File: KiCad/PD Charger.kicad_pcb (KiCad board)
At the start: 4 copper layers, 75 x 40 mm, 89 parts, among them J1 USB_C_Receptacle_USB2.0, J2 Conn_ARM_SWD_TagConnect_TC2030, J3 XT60_M, Q1 NMOS, Q2 NMOS, Q3 NMOS, Q4 NMOS, Q5 NTMFS002P03, Q6 NTMFS002P03, Q7 Q_Dual_NMOS_S1G1D2S2G2D1, Q8 Q_Dual_NMOS_S1G1D2S2G2D1, SW1 SW_MEC_5G, U1 FUSB302B01MPX, U2 LMR36006BRNXT, U3 LT8390xFE, U4 STM32G431C6Ux

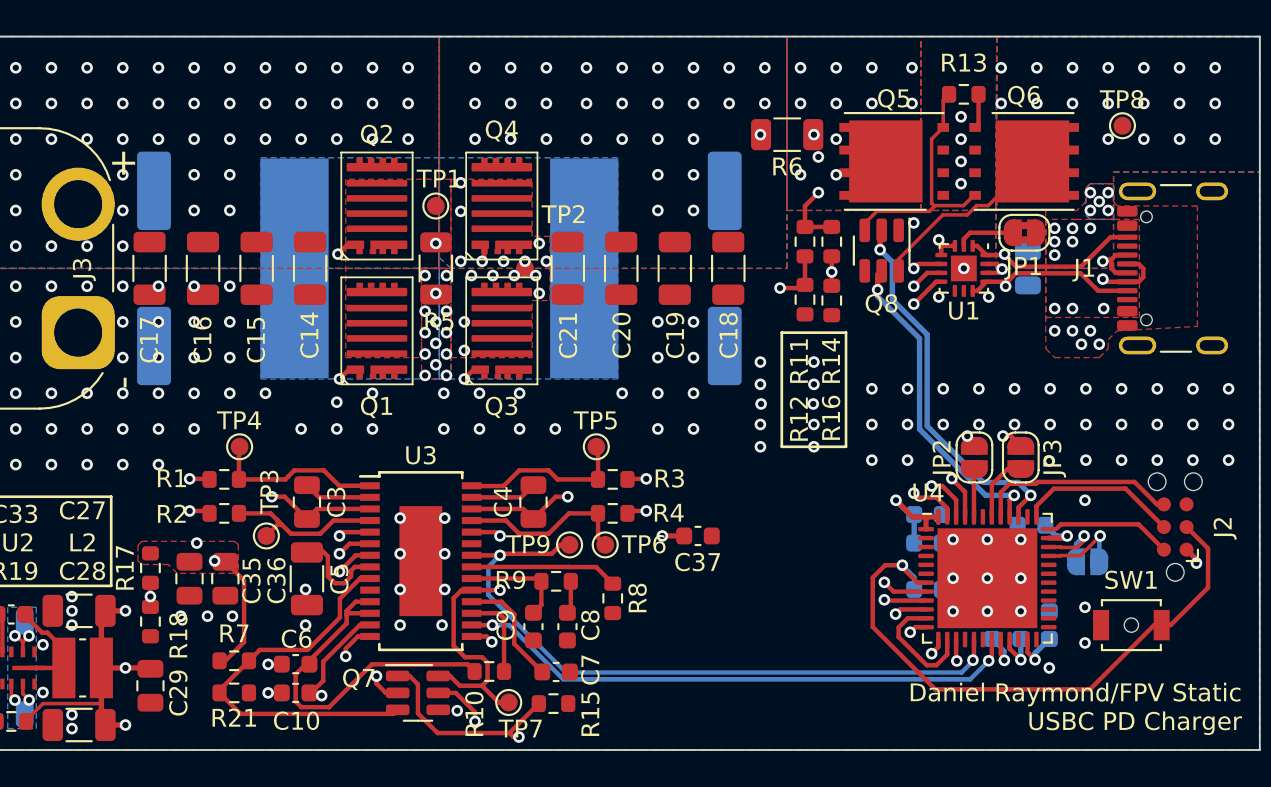
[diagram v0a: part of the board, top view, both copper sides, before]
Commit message: board update from tested issues
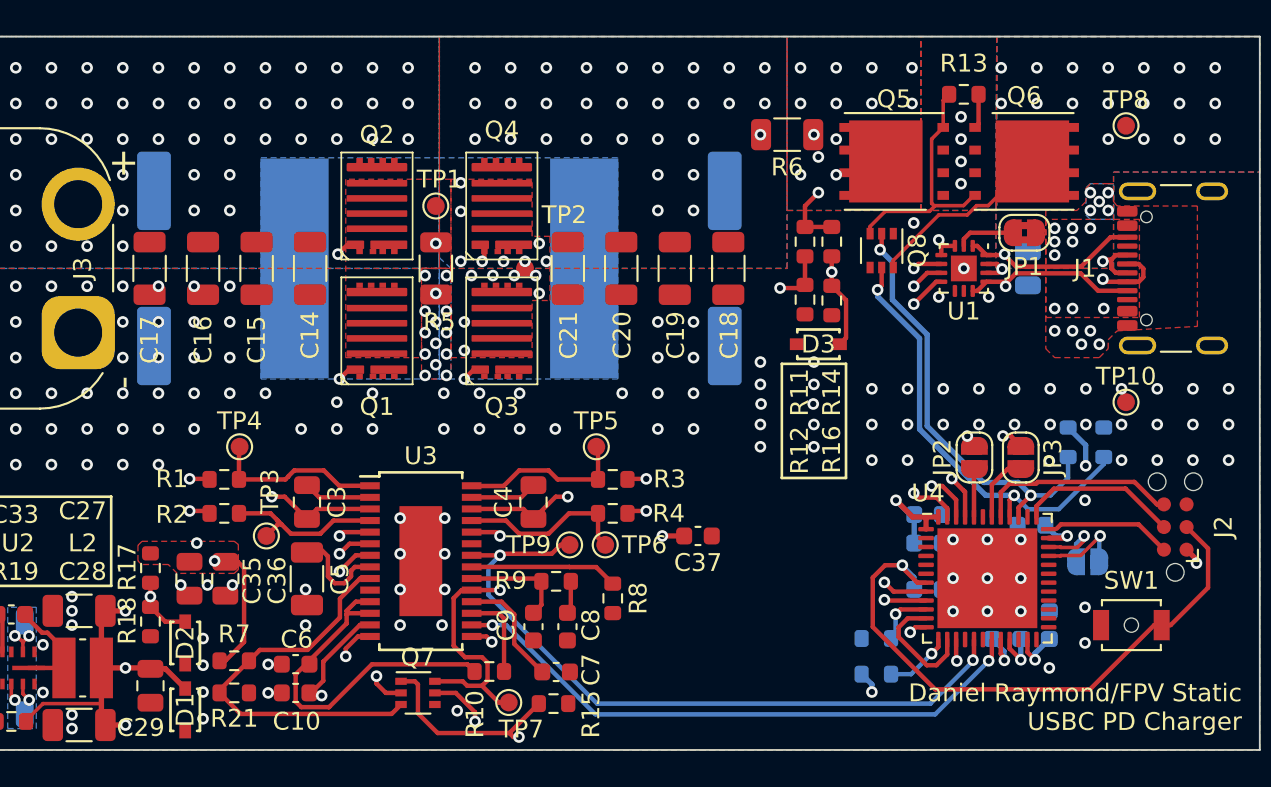
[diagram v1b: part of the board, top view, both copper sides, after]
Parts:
- added D1: 3.425, Library:CR_PLZ5V1C_VIS, F.Cu at (26.8, 49.8)
- added D2: 3.425, Library:CR_PLZ5V1C_VIS, F.Cu at (26.8, 46.0)
- added D3: 3.425, Library:CR_PLZ5V1C_VIS, F.Cu at (62.2, 29.2)
- added R22: 100k, Resistor_SMD:R_0603_1608Metric, B.Cu at (78.2, 34.8)
- added R23: 100k, Resistor_SMD:R_0603_1608Metric, B.Cu at (76.2, 34.8)
- added R24: 100k, Resistor_SMD:R_0603_1608Metric, B.Cu at (65.5, 47.8)
- added R25: 100k, Resistor_SMD:R_0603_1608Metric, B.Cu at (65.5, 45.8)
- added TP10: TestPoint_Small, TestPoint:TestPoint_Pad_D1.0mm, F.Cu at (79.5, 32.5)
- Q7, Q8: footprint Package_TO_SOT_SMD:SOT-23-6 -> Package_TO_SOT_SMD:SOT-363_SC-70-6
- moved TP8 0.20 mm to (79.5, 17.0)
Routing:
- net +3V3: track 128.1 -> 146.2 mm, vias 10 -> 12
- net /LOADEN: track 18.1 -> 25.1 mm
- net /VOUT_SENSE: track 24.1 -> 27.9 mm
- net /OUTDIS: track 21.0 -> 24.5 mm
- net /~{RUN}: track 31.2 -> 33.9 mm
- net /VIN_SENSE: track 48.7 -> 51.0 mm
- net /ISMON: track 31.9 -> 33.6 mm
- net /VCTRLV: track 34.2 -> 35.7 mm
- net /SYNC: track 38.7 -> 40.1 mm
- net GND: vias 160 -> 163

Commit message: board update
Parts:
- added R26: 10k, Resistor_SMD:R_0603_1608Metric, F.Cu at (85.2, 39.0)
- added R27: 10k, Resistor_SMD:R_0603_1608Metric, F.Cu at (85.2, 42.2)
- added SW2: SW_MEC_5G, Button_Switch_SMD:SW_SPST_B3U-1000P-B, F.Cu at (82.8, 45.5)
- moved R22 7.62 mm to (71.2, 37.8), turned to 180 degrees
- moved R23 3.01 mm to (76.0, 37.8), turned to 0 degrees
- moved JP4 2.18 mm to (75.2, 41.8), turned to -90 degrees
- moved C12 1.06 mm to (68.2, 39.4)
- moved C13 1.06 mm to (68.2, 37.8)
- moved SW1 0.74 mm to (79.2, 45.5), turned to 90 degrees
- moved JP1 0.20 mm to (74.0, 23.0)
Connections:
- R24 pad 1: +3V3 -> GND
- U3 pad 11: /VREF -> /REGEN
- U4 pad 2: unconnected-(U4-PC13-Pad2) -> /REGEN
- U4 pad 30: unconnected-(U4-PA8-Pad30) -> /SDA
- U4 pad 31: unconnected-(U4-PA9-Pad31) -> /SCL
- U4 pad 32: unconnected-(U4-PA10-Pad32) -> /INT_N
- U4 pad 45: /SDA -> unconnected-(U4-PB7-Pad45)
- U4 pad 46: /SCL -> /BOOT0
- U4 pad 47: /INT_N -> unconnected-(U4-PB9-Pad47)
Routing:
- net /REGEN: track 0.00 -> 39.9 mm, vias 0 -> 2
- net /BOOT0: track 0.00 -> 33.2 mm
- net /SDA: track 15.3 -> 28.5 mm
- net /INT_N: track 18.1 -> 30.8 mm
- net /SCL: track 16.8 -> 28.9 mm
- net +3V3: track 146.2 -> 139.4 mm, vias 12 -> 11
- net IS: track 56.3 -> 61.6 mm
- net /LOADEN: track 25.1 -> 20.2 mm
- net Net-(R27-Pad1): track 0.00 -> 2.80 mm
- net /USB_DN: track 28.9 -> 31.4 mm
- net /CC1: track 20.3 -> 22.8 mm
- net /OUTDIS: track 24.5 -> 22.3 mm
- net /VREF: track 20.4 -> 18.4 mm
- net /~{RST}: track 34.7 -> 36.2 mm
- net /CC2: track 23.5 -> 24.9 mm
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
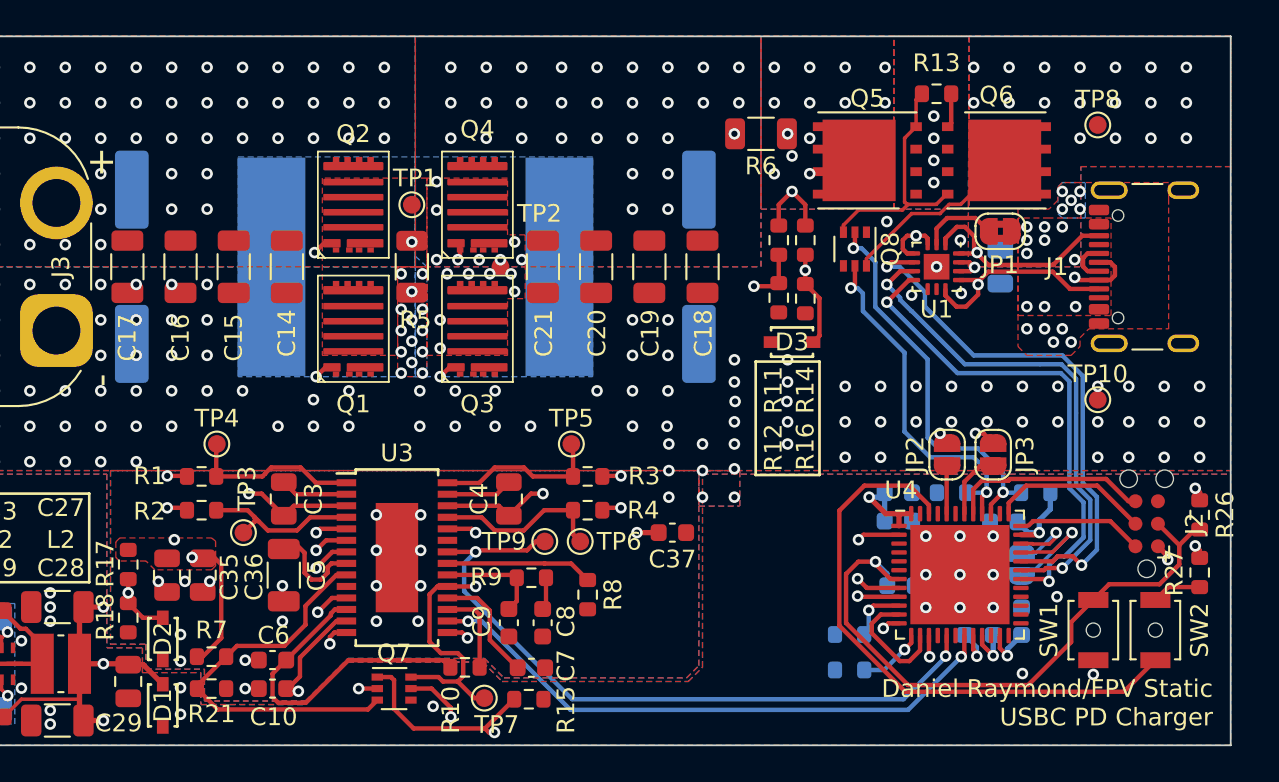
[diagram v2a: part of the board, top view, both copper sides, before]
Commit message: better usbc & fusb302 routing
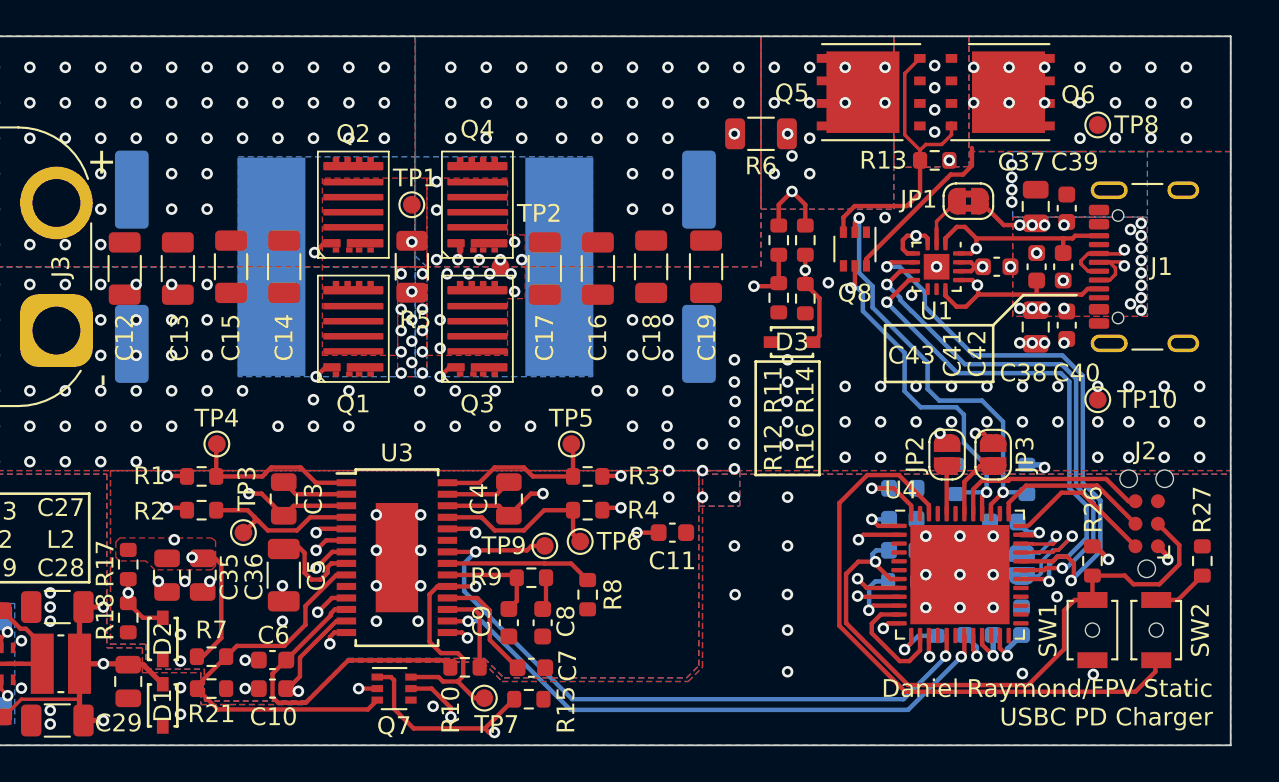
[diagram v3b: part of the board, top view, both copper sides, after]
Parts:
- added C38: 0.47u, Capacitor_SMD:C_0805_2012Metric, F.Cu at (76.0, 28.4)
- added C39: 100n, Capacitor_SMD:C_0603_1608Metric, F.Cu at (77.8, 21.7)
- added C40: 100n, Capacitor_SMD:C_0603_1608Metric, F.Cu at (77.8, 28.3)
- added C41: 330p, Capacitor_SMD:C_0603_1608Metric, F.Cu at (76.0, 25.0)
- added C42: 330p, Capacitor_SMD:C_0603_1608Metric, F.Cu at (77.5, 25.0)
- added C43: 100n, Capacitor_SMD:C_0603_1608Metric, F.Cu at (73.8, 25.0)
- C11: value 100n -> 1u; moved to F.Cu
- C12, C13: value 0.1u -> 10u; footprint Capacitor_SMD:C_0603_1608Metric -> Capacitor_SMD:C_1206_3216Metric; moved to F.Cu
- C20, C21: value 10u -> 0.1u; footprint Capacitor_SMD:C_1206_3216Metric -> Capacitor_SMD:C_0603_1608Metric; moved to B.Cu
- C22: value 0.47u -> 0.1u; footprint Capacitor_SMD:C_0805_2012Metric -> Capacitor_SMD:C_0603_1608Metric
- C24: value 0.1u -> 0.47u
- C25: value 0.47u -> 100n
- C37: value 1u -> 0.47u; footprint Capacitor_SMD:C_0603_1608Metric -> Capacitor_SMD:C_0805_2012Metric
- U4: value STM32G431C6Ux -> STM32G431CBUx
- moved C12 45.9 mm to (24.6, 25.1), turned to -90 degrees
- moved C13 42.6 mm to (27.6, 25.1), turned to -90 degrees
- moved C37 27.5 mm to (76.0, 21.6), turned to 90 degrees
- moved C21 24.8 mm to (68.5, 39.2), turned to 0 degrees
- moved C16 23.6 mm to (51.3, 25.1)
- moved C17 23.6 mm to (48.3, 25.1)
- moved C20 21.3 mm to (68.5, 37.5), turned to 0 degrees
- moved C22 14.4 mm to (74.2, 39.4), turned to 180 degrees
- moved C11 13.2 mm to (55.5, 40.0)
- moved R26 6.59 mm to (79.2, 41.6)
- moved C23 5.69 mm to (75.2, 45.0), turned to 90 degrees
- moved R24 5.62 mm to (70.4, 45.0), turned to -90 degrees
- moved C26 5.32 mm to (68.5, 41.0), turned to 0 degrees
- moved R25 4.24 mm to (68.5, 42.8), turned to 0 degrees
- moved Q5 3.86 mm to (66.7, 15.2)
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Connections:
- C11 pad 1: /~{RST} -> VD
- C12 pad 1: +3V3 -> VS
- C13 pad 1: +3V3 -> VS
- C16 pad 1: VS -> IS
- C17 pad 1: VS -> IS
- C20 pad 1: IS -> +3V3
- C21 pad 1: IS -> +3V3
- C22 pad 1: GND -> +3V3
- C22 pad 2: /VBUS -> GND
- C25 pad 1: +3V3 -> /VREF+
- C26 pad 1: /VREF+ -> /~{RST}
- C37 pad 1: VD -> VBUS
- J1 pad A4: /VBUS -> VBUS
- J1 pad A9: /VBUS -> VBUS
- J1 pad B4: /VBUS -> VBUS
- J1 pad B9: /VBUS -> VBUS
- JP1 pad 2: /VBUS -> VBUS
- Q6 pad 5: /VBUS -> VBUS
- Q8 pad 6: /VBUS -> VBUS
- TP8 pad 1: /VBUS -> VBUS
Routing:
- net VBUS: track 0.00 -> 12.3 mm, vias 0 -> 36
- net /VBUS: track 10.5 -> 0.00 mm, vias 27 -> 0
- net +3V3: track 139.4 -> 144.4 mm, vias 11 -> 13
- net Net-(Q5-G): track 13.8 -> 16.9 mm
- net /USB_DN: track 31.4 -> 29.4 mm
- net /COM_S: track 1.94 -> 0.00 mm, vias 4 -> 5
- net /INT_N: track 30.8 -> 32.7 mm
- net /OUTDIS: track 22.3 -> 24.1 mm
- net Net-(JP1-A): track 4.39 -> 2.91 mm
- net /SWDIO: track 6.72 -> 8.04 mm
- net /USB_DP: track 28.7 -> 27.5 mm
- net /BOOT0: track 33.2 -> 34.3 mm
- net /VCTRLV: track 34.8 -> 35.8 mm
- net GND: track 0.89 -> 0.11 mm, vias 171 -> 177
- net /CC2: track 24.9 -> 25.6 mm
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- added copper zone on B.Cu, net VBUS
- added copper zone on F.Cu, net VBUS
- added copper zone on In1.Cu, net VBUS
- removed copper zone on B.Cu, net /VBUS
- removed copper zone on F.Cu, net /VBUS
- removed copper zone on In2.Cu, net /VBUS

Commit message: new layout
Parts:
- removed JP1: SolderJumper_2_Bridged, Jumper:SolderJumper-2_P1.3mm_Bridged2Bar_RoundedPad1.0x1.5mm
- removed JP2, JP4: SolderJumper_2_Open, Jumper:SolderJumper-2_P1.3mm_Open_RoundedPad1.0x1.5mm
- added C44: 1uF, Capacitor_SMD:C_0603_1608Metric, F.Cu at (17.0, 25.0)
- added C45: 20nF, Capacitor_SMD:C_0603_1608Metric, F.Cu at (24.5, 14.0)
- added C46: 50nF, Capacitor_SMD:C_0603_1608Metric, F.Cu at (23.0, 14.0)
- added C47: 1uF, Capacitor_SMD:C_0603_1608Metric, F.Cu at (13.0, 15.5)
- added C48: 1n, Capacitor_SMD:C_0603_1608Metric, F.Cu at (17.0, 19.5)
- added D4: 22, Library:CR_PLZ5V1C_VIS, F.Cu at (67.4, 55.2)
- added HS1: 960-21-18-D-AB-0, Library:960-21-xx-D, B.Cu at (49.0, 35.0)
- added NT5: NetTie_2, NetTie:NetTie-2_SMD_Pad0.5mm, F.Cu at (30.2, 13.2)
- added NT6: NetTie_2, NetTie:NetTie-2_SMD_Pad0.5mm, F.Cu at (19.2, 52.5)
- added Q9: Q_Dual_NMOS_S1G1D2S2G2D1, Package_TO_SOT_SMD:SOT-363_SC-70-6, F.Cu at (74.7, 50.2)
- added R28: 100k, Resistor_SMD:R_0603_1608Metric, F.Cu at (18.5, 14.0)
- added R29: 4.3k, Resistor_SMD:R_0603_1608Metric, F.Cu at (20.0, 14.0)
- added R30: 100k, Resistor_SMD:R_0603_1608Metric, F.Cu at (15.5, 14.0)
- added R31: 100k, Resistor_SMD:R_0603_1608Metric, F.Cu at (17.0, 14.0)
- added R32: 29k, Resistor_SMD:R_0603_1608Metric, F.Cu at (21.5, 14.0)
- added R33: 0, Resistor_SMD:R_0603_1608Metric, F.Cu at (20.0, 25.0)
- added R34: 68k, Resistor_SMD:R_0603_1608Metric, F.Cu at (21.5, 25.0)
- added R35: 1.2k, Resistor_SMD:R_0603_1608Metric, F.Cu at (23.0, 25.0)
- added R36: 10, Resistor_SMD:R_0603_1608Metric, F.Cu at (18.0, 22.0)
- added R37: 10, Resistor_SMD:R_0603_1608Metric, F.Cu at (18.0, 17.0)
- added R38: 100k, Resistor_SMD:R_0603_1608Metric, F.Cu at (24.5, 25.0)
- added R39: 2k, Resistor_SMD:R_0603_1608Metric, F.Cu at (70.9, 55.8)
- added R40: 2k, Resistor_SMD:R_0603_1608Metric, F.Cu at (72.4, 55.8)
- added R41: 2k, Resistor_SMD:R_0603_1608Metric, F.Cu at (73.9, 55.8)
- added R42: 22k, Resistor_SMD:R_0603_1608Metric, F.Cu at (67.4, 51.2)
- added TP11: TestPoint_Small, TestPoint:TestPoint_Pad_D1.0mm, F.Cu at (28.6, 84.0)
- added U5: ADM1270ACPZ, Package_CSP:LFCSP-16-1EP_3x3mm_P0.5mm_EP1.5x1.5mm, F.Cu at (22.0, 19.5)
- added U6: INA293A2, Package_TO_SOT_SMD:SOT-23-5, F.Cu at (14.0, 19.5)
- added U7: TPD4E05U06DQA, Package_SON:USON-10_2.5x1.0mm_P0.5mm, F.Cu at (70.9, 45.2)
- C1, C2: value 82u -> 10u; footprint Capacitor_SMD:CP_Elec_10x7.9 -> Capacitor_SMD:C_1206_3216Metric; moved to F.Cu
- C10: value 4.7u -> 0.47u; footprint Capacitor_SMD:C_0603_1608Metric -> Capacitor_SMD:C_0805_2012Metric
- C14, C15: value 10u -> 82u; footprint Capacitor_SMD:C_1206_3216Metric -> Capacitor_SMD:CP_Elec_10x7.9
- C20, C21: value 0.1u -> 100n; moved to F.Cu
- C22, C23, L1, R23: moved to F.Cu
- C24: value 0.47u -> 0.1u; moved to F.Cu
- C25: value 100n -> 0.1u; moved to F.Cu
- C26: value 100n -> 0.47u; moved to F.Cu
- C27, C28: value 10u -> 0.47u; footprint Capacitor_SMD:C_1206_3216Metric -> Capacitor_SMD:C_0805_2012Metric
- C29: value 0.47u -> 1u; footprint Capacitor_SMD:C_0805_2012Metric -> Capacitor_SMD:C_0603_1608Metric
- C3: value 0.47u -> 10u; footprint Capacitor_SMD:C_0805_2012Metric -> Capacitor_SMD:C_1206_3216Metric
- C30: value 0.47u -> 100n; footprint Capacitor_SMD:C_0805_2012Metric -> Capacitor_SMD:C_0603_1608Metric; moved to F.Cu
- C31: value 0.47u -> 20p; footprint Capacitor_SMD:C_0805_2012Metric -> Capacitor_SMD:C_0603_1608Metric; moved to F.Cu
- C32: value 1u -> 10u; footprint Capacitor_SMD:C_0603_1608Metric -> Capacitor_SMD:C_1206_3216Metric
- C33: value 100n -> 10u; footprint Capacitor_SMD:C_0603_1608Metric -> Capacitor_SMD:C_1206_3216Metric
- C34: value 20p -> 0.47u; footprint Capacitor_SMD:C_0603_1608Metric -> Capacitor_SMD:C_0805_2012Metric
- C37: value 0.47u -> 100n; footprint Capacitor_SMD:C_0805_2012Metric -> Capacitor_SMD:C_0603_1608Metric
- C39: value 100n -> 0.47u; footprint Capacitor_SMD:C_0603_1608Metric -> Capacitor_SMD:C_0805_2012Metric
- C4: footprint Capacitor_SMD:C_0805_2012Metric -> Capacitor_SMD:C_0603_1608Metric
- C41: value 330p -> 100n
- C43: value 100n -> 330p
- C5: value 10u -> 4.7n; footprint Capacitor_SMD:C_1206_3216Metric -> Capacitor_SMD:C_0603_1608Metric
- C6: value 0.47u -> 100p
- C7: value 0.1u -> 4.7n
- C8: value 4.7n -> 0.1u
- C9: value 100p -> 0.47u; footprint Capacitor_SMD:C_0603_1608Metric -> Capacitor_SMD:C_0805_2012Metric
- J2, JP3, Q1, Q2, Q3, Q4: moved to B.Cu
- Q5, Q6: value NTMFS002P03 -> SiR5607DP
- Q7, Q8: value Q_Dual_NMOS_S1G1D2S2G2D1 -> SiR5607DP; footprint Package_TO_SOT_SMD:SOT-363_SC-70-6 -> Package_DFN_QFN:AO_DFN-8-1EP_5.55x5.2mm_P1.27mm_EP4.12x4.6mm
- R1, R4: value 1 -> 100k
- R10: value 100k -> 1
- R11: value 36k -> 1
- R12: value 9k -> 1
- R15: value 752 -> 36k
- R2: value 1 -> 27k
- R21: value 33k -> 9k
- R22: value 100k -> ~; moved to F.Cu
- R24: value 100k -> 0; moved to F.Cu
- R25: value 100k -> 2m; footprint Resistor_SMD:R_0603_1608Metric -> Resistor_SMD:R_Shunt_Ohmite_LVK12; moved to F.Cu
- R3: value 1 -> 33k
- R5: footprint Resistor_SMD:R_1206_3216Metric -> Resistor_SMD:R_Shunt_Ohmite_LVK12
- R6: value 20m -> 12m; footprint Resistor_SMD:R_1206_3216Metric -> Resistor_SMD:R_Shunt_Ohmite_LVK12
- R9: value 27k -> 1
- moved TP2 64.6 mm to (19.5, 84.0)
- moved TP1 63.2 mm to (19.5, 81.0)
- moved R24 55.6 mm to (18.5, 25.0), turned to 90 degrees
- moved TP5 52.0 mm to (25.6, 81.0)
- moved TP6 50.1 mm to (25.6, 84.0)
- moved TP4 49.6 mm to (22.6, 84.0)
- moved R25 48.3 mm to (28.0, 16.5), turned to 180 degrees
- moved TP3 41.9 mm to (22.6, 81.0)
- moved R17 41.1 mm to (64.5, 52.3)
- moved R18 41.1 mm to (64.5, 55.3)
- moved R14 40.5 mm to (34.5, 52.3)
- moved R16 40.3 mm to (34.5, 55.3)
- moved TP7 35.6 mm to (28.6, 81.0)
- moved C37 34.8 mm to (69.4, 55.8), turned to -90 degrees
- moved Q8 33.3 mm to (33.5, 15.9), turned to 0 degrees
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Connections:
- net /BOOT0 renamed /MCU/BOOT0
- net /COM_S renamed /Output Switch/COM_S
- net /INT_N renamed /~{INT}
- net /RT renamed /DC-DC/RT
- net /SWCLK renamed /MCU/SWCLK
- net /SWDIO renamed /MCU/SWDIO
- net /SWO renamed /MCU/SWO
- C10 pad 1: /VCTRLI -> /DC-DC/SW2
- C10 pad 2: GND -> /DC-DC/BST2
- C15 pad 1: VS -> /DC-DC/VOUTa
- C16 pad 1: IS -> /DC-DC/VOUTa
- C17 pad 1: IS -> /DC-DC/VOUTa
- C18 pad 1: IS -> /DC-DC/VOUTa
- C19 pad 1: IS -> /DC-DC/VOUTa
- C2 pad 1: IS -> VS
- C20 pad 1: +3V3 -> /MCU/VREF+
- C21 pad 1: +3V3 -> /MCU/~{RST}
- C25 pad 1: /VREF+ -> +3V3
- C26 pad 1: /~{RST} -> +3V3
- C27 pad 1: +3V3 -> GND
- C27 pad 2: GND -> /VS_NO_LIM
- C28 pad 1: +3V3 -> GND
- C28 pad 2: GND -> /VS_NO_LIM
- C29 pad 1: GND -> /3v3 Regulator/VCC
- C29 pad 2: +3V3 -> GND
- C3 pad 1: Net-(U3-BST1) -> /DC-DC/VDD
- C3 pad 2: SW1 -> GND
- C30 pad 1: GND -> /3v3 Regulator/BST
- C30 pad 2: VS -> Net-(U2-SW)
- C31 pad 1: GND -> /3v3 Regulator/FB
- C31 pad 2: VS -> GND
- C32 pad 1: Net-(U2-VCC) -> +3V3
- C33 pad 1: Net-(U2-BST) -> +3V3
- C33 pad 2: Net-(U2-SW) -> GND
- C34 pad 1: Net-(U2-FB) -> GND
- C34 pad 2: GND -> +3V3
- C37 pad 1: VBUS -> +3V3
- C4 pad 1: SW2 -> /DC-DC/VREF
- C4 pad 2: Net-(U3-BST2) -> GND
- C41 pad 1: /CC1 -> VBUS
- C42 pad 1: /CC2 -> /CC
- C43 pad 1: +3V3 -> /VCONN
- C5 pad 1: VDD -> /ICTRL
- C6 pad 1: /VREF -> /DC-DC/VC
- C7 pad 1: /SS -> Net-(C7-Pad1)
- C8 pad 1: Net-(C8-Pad1) -> /DC-DC/SS
- C9 pad 1: /VC -> /DC-DC/BST1
- C9 pad 2: GND -> /DC-DC/SW1
- D2 pad 1: /VIN_SENSE -> /VSMON
- D3 pad 1: /VOUT_SENSE -> /VDMON
- J1 pad A5: /CC1 -> /CC
- J1 pad B5: /CC2 -> /VCONN
- J2 pad 3: /~{RST} -> /MCU/~{RST}
- J3 pad 2: VS -> VIN
- JP3 pad 1: /CC2 -> /USB_DP
- JP3 pad 2: Net-(JP3-B) -> /USB_DN
- L1 pad 1: LS -> /DC-DC/SW1a
- L1 pad 2: SW2 -> /DC-DC/SW2
- Q1 pad 1: SW1 -> VS
- Q1 pad 2: /G1 -> /DC-DC/G1
- Q1 pad 3: GND -> /DC-DC/SW1
- Q2 pad 1: VS -> /DC-DC/SW1
- Q2 pad 2: /G2 -> /DC-DC/G2
- Q2 pad 3: SW1 -> GND
- Q3 pad 1: SW2 -> /DC-DC/VOUTa
- Q3 pad 2: /G3 -> /DC-DC/G3
- Q3 pad 3: GND -> /DC-DC/SW2
- Q4 pad 1: IS -> /DC-DC/SW2
- Q4 pad 2: /G4 -> /DC-DC/G4
- Q4 pad 3: SW2 -> GND
- Q5 pad 4: Net-(Q5-G) -> /DC-DC/LOADTG
- Q6 pad 4: Net-(Q5-G) -> /DC-DC/LOADTG
- Q7 pad 1: /VADJ -> /Input Protection/Q7_S
- Q7 pad 2: /VCTRLV -> /Input Protection/Q7_S
- Q7 pad 3: /EN -> /Input Protection/Q7_S
- Q7 pad 4: GND -> /Input Protection/G_RP
- Q7 pad 5: /~{RUN} -> VIN
- Q8 pad 1: GND -> /Input Protection/Q8_S
- Q8 pad 2: /OUTDIS -> /Input Protection/Q8_S
- Q8 pad 3: Net-(Q5-G) -> /Input Protection/Q8_S
- Q8 pad 4: GND -> /Input Protection/G_BP
- Q8 pad 5: /LOADEN -> VS
- R1 pad 1: Net-(U3-BG1) -> /DC-DC/VREF
- R1 pad 2: /G1 -> /DC-DC/~{PGOOD}
- R10 pad 1: /VREF -> /DC-DC/BG1
- R10 pad 2: /~{PGOOD} -> /DC-DC/G2
- R11 pad 1: /FB -> /DC-DC/BG2
- R11 pad 2: VD -> /DC-DC/G4
- R12 pad 1: GND -> /DC-DC/TG2
- R12 pad 2: /FB -> /DC-DC/G3
- R13 pad 2: Net-(Q5-G) -> /DC-DC/LOADTG
- R14 pad 1: VD -> VS
- R14 pad 2: /VOUT_SENSE -> /VSMON
- R15 pad 1: /VADJ -> /DC-DC/FB
- R15 pad 2: GND -> VD
- R16 pad 1: /VOUT_SENSE -> /VSMON
- R17 pad 1: VS -> VD
- R17 pad 2: /VIN_SENSE -> /VDMON
- R18 pad 1: /VIN_SENSE -> /VDMON
- R19 pad 2: Net-(U2-FB) -> /3v3 Regulator/FB
- R2 pad 1: Net-(U3-TG1) -> /DC-DC/VC
- R2 pad 2: /G2 -> Net-(C7-Pad1)
- R20 pad 1: Net-(U2-FB) -> /3v3 Regulator/FB
- R21 pad 2: /EN -> /DC-DC/FB
- R22 pad 1: /LOADEN -> /DC-DC/FB
- R22 pad 2: GND -> /VCTRL
- R23 pad 1: /OUTDIS -> /LOAD_DISCHRG
- R24 pad 1: GND -> /Input Protection/VCAP
- R24 pad 2: /~{RUN} -> /Input Protection/ISET
- R25 pad 1: /VCTRLV -> /Input Protection/Q7_S
- R25 pad 2: GND -> /Input Protection/SENSE+
- R26 pad 1: +3V3 -> Net-(R26-Pad1)
- R26 pad 2: /~{RST} -> GND
- R27 pad 1: Net-(R27-Pad1) -> +3V3
- R27 pad 2: GND -> /MCU/~{RST}
- R3 pad 1: Net-(U3-BG2) -> GND
- R3 pad 2: /G3 -> /DC-DC/UVLO
- R4 pad 1: Net-(U3-TG2) -> /LOADEN
- R4 pad 2: /G4 -> GND
- R5 pad 1: SW1 -> /DC-DC/SW1a
- R5 pad 2: LS -> /DC-DC/LSN
- R6 pad 1: VD -> /DC-DC/VOUTa
- R6 pad 2: IS -> /DC-DC/ISP
- R7 pad 2: /EN -> /DC-DC/UVLO
- R9 pad 1: /VC -> /DC-DC/TG1
- R9 pad 2: Net-(C8-Pad1) -> /DC-DC/G1
- SW1 pad 2: /~{RST} -> /MCU/~{RST}
- SW2 pad 1: Net-(R27-Pad1) -> Net-(R26-Pad1)
- TP1 pad 1: SW1 -> /DC-DC/G1
- TP2 pad 1: SW2 -> /DC-DC/SW1
- TP3 pad 1: Net-(U3-TG1) -> /DC-DC/G2
- TP4 pad 1: Net-(U3-BG1) -> /DC-DC/G4
- TP5 pad 1: Net-(U3-BG2) -> /DC-DC/SW2
- TP6 pad 1: Net-(U3-TG2) -> /DC-DC/G3
- TP7 pad 1: /FB -> /VCTRL
- U1 pad 1: /CC2 -> /VCONN
- U1 pad 10: /CC1 -> /CC
- U1 pad 11: /CC1 -> /CC
- U1 pad 14: /CC2 -> /VCONN
- U1 pad 2: Net-(JP1-A) -> /USB-C/VBUS_LIM
- U2 pad 10: VS -> /VS_NO_LIM
- U2 pad 2: VS -> /VS_NO_LIM
- U2 pad 4: Net-(U2-BST) -> /3v3 Regulator/BST
- U2 pad 5: Net-(U2-VCC) -> /3v3 Regulator/VCC
- U2 pad 7: Net-(U2-FB) -> /3v3 Regulator/FB
- U2 pad 9: VS -> /3v3 Regulator/EN
- U3 pad 1: Net-(U3-BG1) -> /DC-DC/BG1
- U3 pad 11: /REGEN -> /LOADEN
- U3 pad 12: /VREF -> /DC-DC/VREF
- U3 pad 13: /VCTRLI -> /ICTRL
- U3 pad 14: IS -> /DC-DC/ISP
- U3 pad 15: VD -> /DC-DC/ISN
- U3 pad 16: /ISMON -> /IDMON
- U3 pad 17: /~{PGOOD} -> /DC-DC/~{PGOOD}
- U3 pad 18: /SS -> /DC-DC/SS
- U3 pad 19: /FB -> /DC-DC/FB
- U3 pad 2: Net-(U3-BST1) -> /DC-DC/BST1
- U3 pad 20: /VC -> /DC-DC/VC
- U3 pad 23: unconnected-(U3-PWMTG-Pad23) -> /DC-DC/LOADTG
- U3 pad 25: Net-(U3-TG2) -> /DC-DC/TG2
- U3 pad 26: SW2 -> /DC-DC/SW2
- U3 pad 27: Net-(U3-BST2) -> /DC-DC/BST2
- U3 pad 28: Net-(U3-BG2) -> /DC-DC/BG2
- U3 pad 3: SW1 -> /DC-DC/SW1
- U3 pad 4: Net-(U3-TG1) -> /DC-DC/TG1
- U3 pad 5: SW1 -> /DC-DC/LSP
- U3 pad 6: LS -> /DC-DC/LSN
- U3 pad 8: VDD -> /DC-DC/VDD
- U3 pad 9: /EN -> /DC-DC/UVLO
- U4 pad 10: /VCTRLV -> /MCU/UART_TX
- U4 pad 11: /VADJ_AMP -> /MCU/UART_RX
- U4 pad 12: /VCTRLI -> /VCTRL
- U4 pad 13: /~{RUN} -> /ICTRL
- U4 pad 14: /VADJ_AMP -> /VDMON
- U4 pad 15: /VADJ -> /IDMON
- U4 pad 16: unconnected-(U4-PC4-Pad16) -> /VSMON
- U4 pad 17: /SYNC -> unconnected-(U4-PB0-Pad17)
- U4 pad 18: /ISAMP -> unconnected-(U4-PB1-Pad18)
- U4 pad 19: /ISMON -> unconnected-(U4-PB2-Pad19)
- U4 pad 2: /REGEN -> /LOAD_DISCHRG
- U4 pad 20: /VREF+ -> /MCU/VREF+
- U4 pad 24: unconnected-(U4-PB11-Pad24) -> /ISMON
- U4 pad 25: unconnected-(U4-PB12-Pad25) -> /MCU/REG_ON
- U4 pad 26: unconnected-(U4-PB13-Pad26) -> /MCU/~{PGOOD}
- U4 pad 27: unconnected-(U4-PB14-Pad27) -> /MCU/SGOOD
- U4 pad 28: unconnected-(U4-PB15-Pad28) -> /MCU/~{FAULT}
- U4 pad 3: unconnected-(U4-PC14-Pad3) -> /LOADEN
- U4 pad 39: /OUTDIS -> unconnected-(U4-PC10-Pad39)
- U4 pad 4: unconnected-(U4-PC15-Pad4) -> /MCU/SOURCE_EN
- U4 pad 40: /LOADEN -> unconnected-(U4-PC11-Pad40)
- U4 pad 42: Net-(JP3-B) -> /VCONN
- U4 pad 44: Net-(JP2-B) -> /CC
- U4 pad 47: unconnected-(U4-PB9-Pad47) -> /SYNC
- U4 pad 7: /~{RST} -> /MCU/~{RST}
- U4 pad 8: /VIN_SENSE -> unconnected-(U4-PA0-Pad8)
- U4 pad 9: /VOUT_SENSE -> unconnected-(U4-PA1-Pad9)
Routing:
- net VD: track 91.2 -> 7.17 mm, vias 17 -> 24
- net /VS_NO_LIM: track 0.00 -> 64.3 mm, vias 0 -> 3
- net IS: track 61.9 -> 0.00 mm, vias 31 -> 0
- net +3V3: track 144.4 -> 88.2 mm, vias 13 -> 7
- net SW1: track 54.7 -> 0.00 mm, vias 3 -> 0
- net /VIN_SENSE: track 51.5 -> 0.00 mm, vias 2 -> 0
- net /FB: track 48.1 -> 0.00 mm, vias 2 -> 0
- net /VCTRLI: track 42.3 -> 0.00 mm, vias 2 -> 0
- net /SYNC: track 40.3 -> 0.00 mm, vias 2 -> 0
- net /REGEN: track 39.9 -> 0.00 mm, vias 2 -> 0
- net /VADJ: track 38.7 -> 0.00 mm, vias 2 -> 0
- net VS: track 60.8 -> 23.9 mm, vias 65 -> 43
- net /~{RST}: track 36.4 -> 0.00 mm, vias 1 -> 0
- net /VCTRLV: track 35.8 -> 0.00 mm, vias 2 -> 0
- net /MCU/BOOT0: track 34.3 -> 0.00 mm
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- added copper zone on F.Cu, net +3V3
- added copper zone on B.Cu, net /DC-DC/SW1
- added copper zone on F.Cu, net /DC-DC/SW1
- added copper zone on F.Cu, net /DC-DC/SW1a
- added copper zone on B.Cu, net /DC-DC/SW2
- added copper zone on F.Cu, net /DC-DC/SW2
- added copper zone on B.Cu, net /DC-DC/VOUTa
- added copper zone on F.Cu, net /DC-DC/VOUTa
- added copper zone on F.Cu, net /Input Protection/Q7_S
- added copper zone on F.Cu, net /Input Protection/Q8_S
- added copper zone on In1.Cu, net VD
- added copper zone on F.Cu, net VIN
- removed copper zone on B.Cu, net /Output Switch/COM_S
- removed copper zone on B.Cu, net GND
- removed copper zone on B.Cu, net IS
- removed copper zone on F.Cu, net IS
- removed copper zone on B.Cu, net LS
- removed copper zone on F.Cu, net LS
- removed copper zone on F.Cu, net SW1
- removed copper zone on B.Cu, net SW2
- removed copper zone on F.Cu, net SW2
- removed copper zone on B.Cu, net VBUS
- removed copper zone on F.Cu, net VBUS
- removed copper zone on In1.Cu, net VBUS
- removed copper zone on B.Cu, net VD
- removed copper zone on In1.Cu, net VS
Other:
- board size 75 x 40 mm -> 74 x 46 mm
- board text removed: "Daniel Raymond/FPV Static USBC PD Charger"
